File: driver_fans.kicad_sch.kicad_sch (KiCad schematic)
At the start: 0 parts

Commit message: Added drived fan circuitry
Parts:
- added FAN1, FAN2: FANCONN, Connector_Molex:Molex_Micro-Fit_3.0_43650-0215_1x02_P3.00mm_Vertical, symbol Connector_Generic:Conn_01x02
- added Q3 (x2): 2N7002, Package_TO_SOT_SMD:SOT-23, symbol Transistor_FET:2N7002
- added R16: 100k, Resistor_SMD:R_0805_2012Metric, symbol Device:R_Small
- added U2: SI8261ABC-IS, Package_SO:SOIC-8_3.9x4.9mm_P1.27mm, symbol utsvt-bps:SI8261ABC-IS
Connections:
- new net +12V: FAN1.1 (Pin_1), FAN2.1 (Pin_1), U2.8 (VDD)
- new net FAN_SIG_12V_1: FAN1.2 (Pin_2), Q3.3 (D)
- new net FAN_SIG_12V_2: FAN2.2 (Pin_2), Q3.3 (D)
- new net FAN_SIG_3V3: U2.2 (ANODE)
- new net GND: U2.3 (CATHODE)
- new net GNDPWR: Q3.2 (S), Q3.2 (S), R16.1, U2.5 (GND)
- new net VO: Q3.1 (G), Q3.1 (G), R16.2, U2.6 (VO), U2.7 (VO)
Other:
- note added: "Driver Fans"

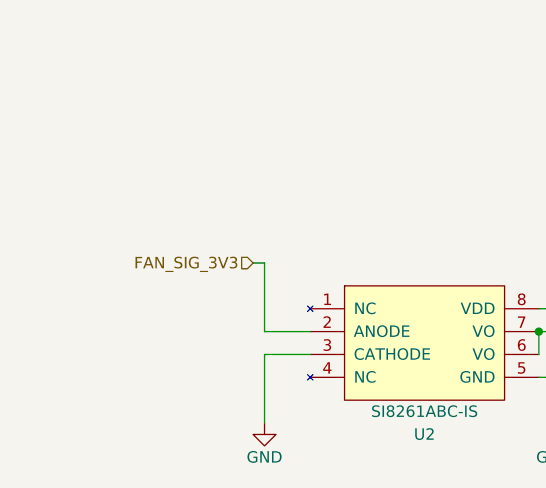
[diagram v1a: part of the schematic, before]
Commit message: Added resistor to fan isolator, fixed ERC errors and warnings
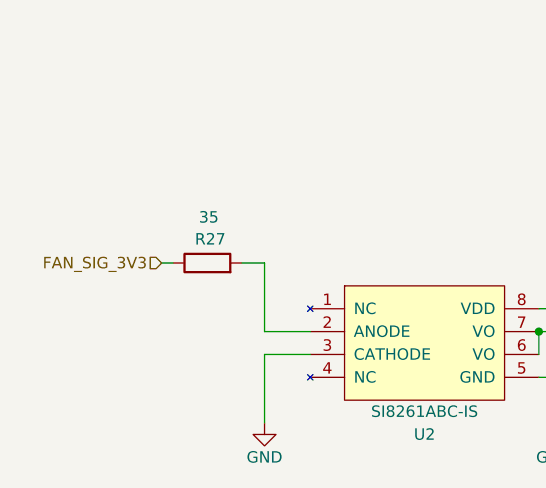
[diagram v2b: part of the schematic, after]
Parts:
- added R27: 35, Resistor_SMD:R_0805_2012Metric, symbol Device:R
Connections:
- net FAN_SIG_3V3: now also R27.1; no longer U2.2 (ANODE)
- new net: R27.2, U2.2 (ANODE)
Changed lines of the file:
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@@
+    (stroke (width 0) (type default))
+  )
+  (wire (pts (xy 57.15 90.17) (xy 58.42 90.17))
     (stroke (width 0) (type default))
   )
@@
     (stroke (width 0) (type default))
   )
-  (wire (pts (xy 67.31 90.17) (xy 68.58 90.17))
+  (wire (pts (xy 66.04 90.17) (xy 68.58 90.17))
     (stroke (width 0) (type default))
   )
@@
     (effects (font (size 1.27 1.27)) (justify right bottom))
   )
-  (hierarchical_label "FAN_SIG_3V3" (shape input) (at 67.31 90.17 180) (fields_autoplaced)
+  (hierarchical_label "FAN_SIG_3V3" (shape input) (at 57.15 90.17 180) (fields_autoplaced)
     (effects (font (size 1.27 1.27)) (justify right))
   )
@@
         )
       )
+    )
+  )
+  (symbol (lib_id "Device:R") (at 62.23 90.17 90) (unit 1)
+    (in_bom yes) (on_board yes) (dnp no)
+    (property "Reference" "R27" (at 64.262 87.5284 90)
+      (effects (font (size 1.27 1.27)) (justify left))
+    )
+    (property "Value" "35" (at 63.5 85.09 90)
+      (effects (font (size 1.27 1.27)) (justify left))
+    )
+    (property "Footprint" "Resistor_SMD:R_0805_2012Metric" (at 62.23 91.948 90)
+      (effects (font (size 1.27 1.27)) hide)
+    )
+    (property "Datasheet" "~" (at 62.23 90.17 0)
+      (effects (font (size 1.27 1.27)) hide)
+    )
+    (property "P/N" "SDR10EZPJ152" (at 62.23 90.17 90)
+      (effects (font (size 1.27 1.27)) hide)
+    )
+    (pin "1")
+    (pin "2")
+    (instances
+      (project "Controls-LightingPCB"
+        (path "/229b82f0-5048-47d6-8bc8-0bcee42eb4bc"
+          (reference "R27") (unit 1)
+        )
+        (path "/229b82f0-5048-47d6-8bc8-0bcee42eb4bc/878def96-76f6-45ed-b005-573a6523d263"
+          (reference "R30") (unit 1)
+        )
+        (path "/229b82f0-5048-47d6-8bc8-0bcee42eb4bc/ceb5a95e-a274-4dea-8a59-96d1af6e854d"
+          (reference "R18") (unit 1)
+        )
+      )
+      (project "Controls-DaughterPCB"
+        (path "/c7871779-04fe-4705-8150-20a4dd0ef44f/f7827f80-0f50-4e4f-b2cd-ff48878538ae"
+          (reference "R16") (unit 1)
+        )
+        (path "/c7871779-04fe-4705-8150-20a4dd0ef44f/fd5723b9-3644-4daa-af29-4c44667f673c"
+          (reference "R32") (unit 1)
+        )
+      )

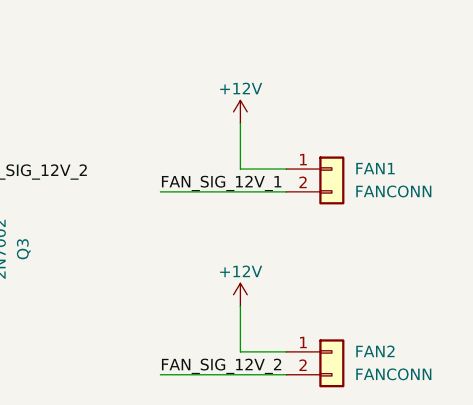
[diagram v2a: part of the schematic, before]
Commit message: changed labels for some connectors
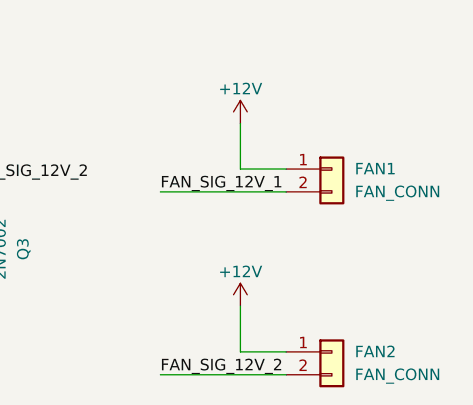
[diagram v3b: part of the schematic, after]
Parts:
- FAN1, FAN2: value FANCONN -> FAN_CONN
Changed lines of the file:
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@@
       (effects (font (size 1.27 1.27)) (justify left))
     )
-    (property "Value" "FANCONN" (at 187.96 91.44 0)
+    (property "Value" "FAN_CONN" (at 187.96 91.44 0)
       (effects (font (size 1.27 1.27)) (justify left))
     )
@@
       (effects (font (size 1.27 1.27)) (justify left))
     )
-    (property "Value" "FANCONN" (at 187.96 111.76 0)
-      (effects (font (size 1.27 1.27)) (justify left))
-    )
+    (property "Value" "FAN_CONN" (at 187.96 111.76 0)
+      (effects (font (size 1.27 1.27)) (justify left))
+    )

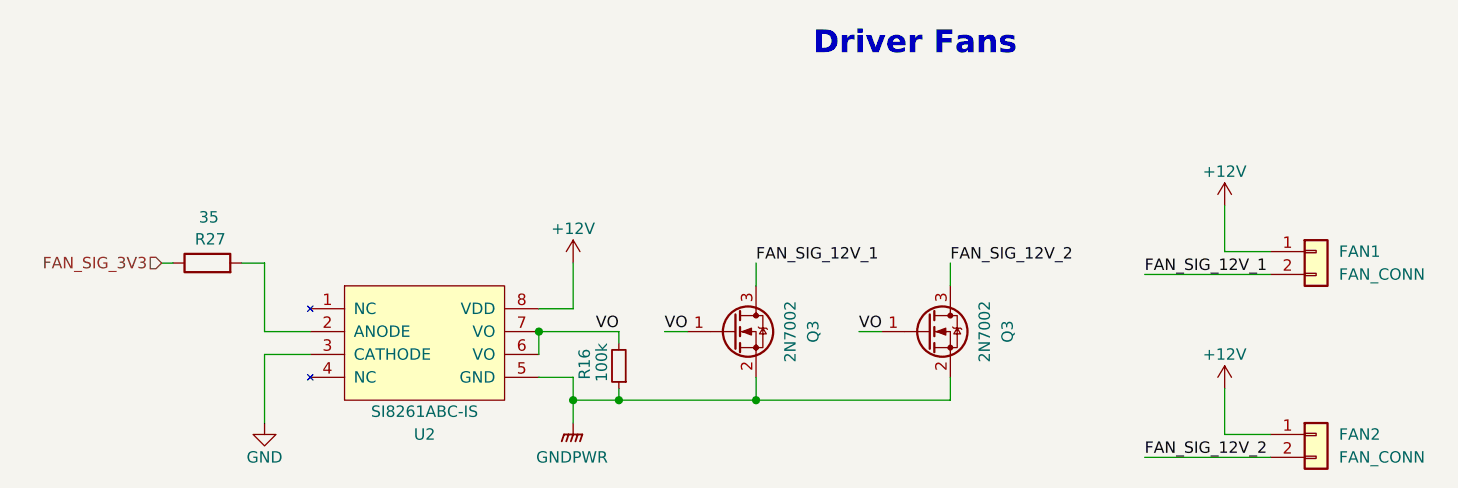
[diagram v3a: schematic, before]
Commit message: lower power optocouplers now used for lights and fans, updated version history
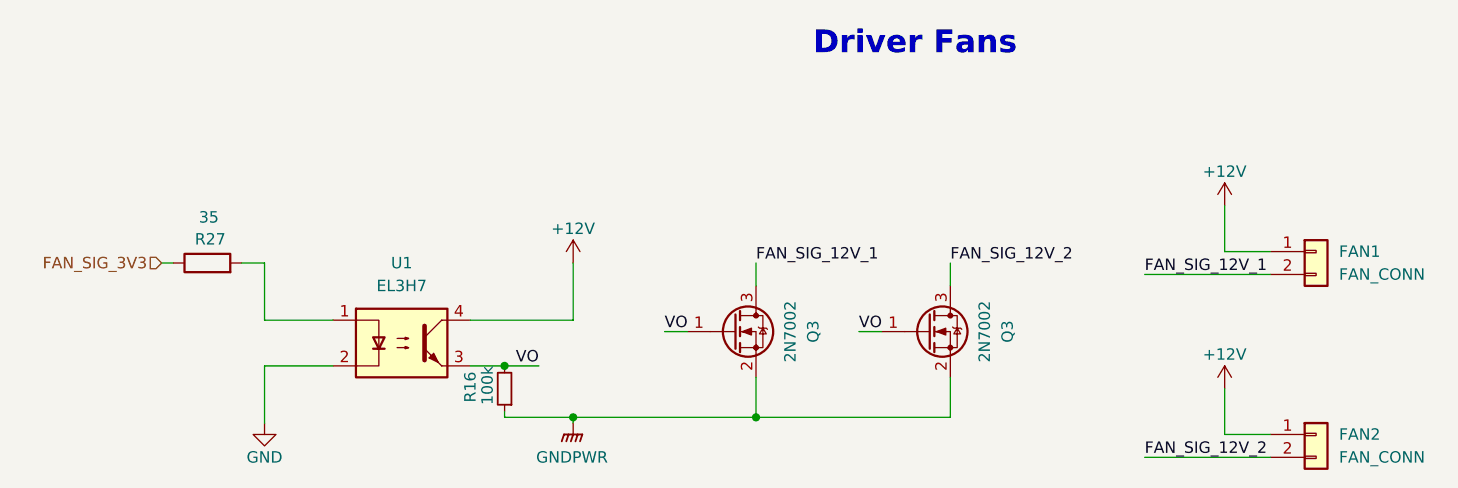
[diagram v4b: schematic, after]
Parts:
- removed U2: SI8261ABC-IS, Package_SO:SOIC-8_3.9x4.9mm_P1.27mm, symbol utsvt-bps:SI8261ABC-IS
- added U1: EL3H7, Package_SO:SOP-4_4.4x2.6mm_P1.27mm, symbol Isolator:EL817
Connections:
- net +12V: now also U1.4
- net GND: now also U1.2
- net VO: now also U1.3
- net at R27.2: now also U1.1
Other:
- moved on the sheet: R16

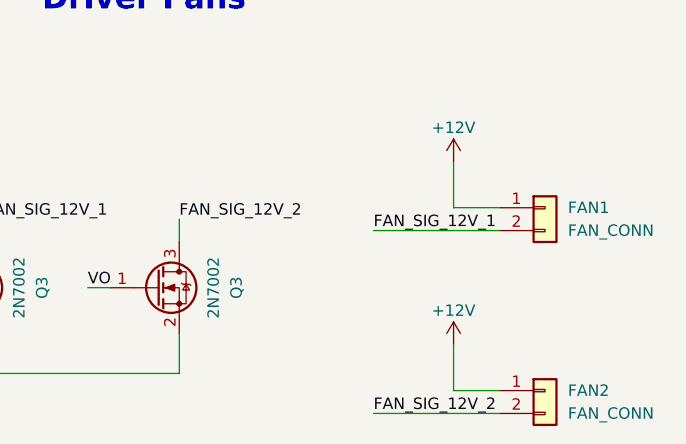
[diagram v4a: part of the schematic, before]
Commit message: Added flyback diodes to fan connectors
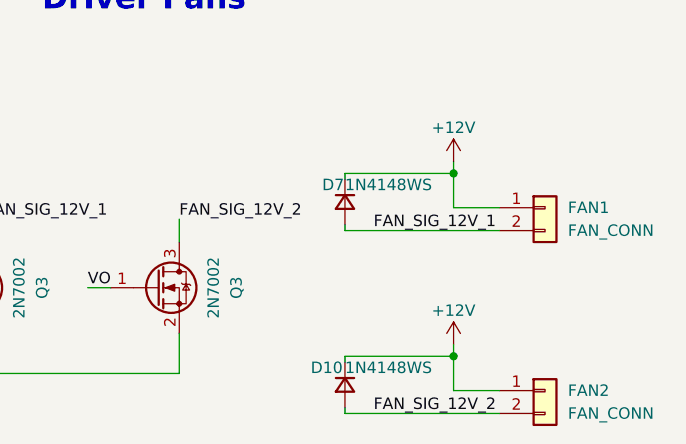
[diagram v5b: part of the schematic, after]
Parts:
- added D10, D7: 1N4148WS, Diode_SMD:D_SOD-323F, symbol Device:D_Small
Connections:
- net +12V: now also D10.1 (K), D7.1 (K)
- net FAN_SIG_12V_1: now also D7.2 (A)
- net FAN_SIG_12V_2: now also D10.2 (A)
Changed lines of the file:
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@@
 (kicad_sch (version 20230121) (generator eeschema)
   (paper "A4")
+  (junction (at 175.26 85.09) (diameter 0) (color 0 0 0 0)
+  )
   (junction (at 95.25 101.6) (diameter 0) (color 0 0 0 0)
   )
@@
   (junction (at 102.87 107.315) (diameter 0) (color 0 0 0 0)
   )
-  (wire (pts (xy 180.34 111.76) (xy 166.37 111.76))
+  (junction (at 175.26 105.41) (diameter 0) (color 0 0 0 0)
+  )
+  (wire (pts (xy 163.195 111.76) (xy 180.34 111.76))
+    (stroke (width 0) (type default))
+  )
+  (wire (pts (xy 163.195 85.09) (xy 163.195 85.725))
+    (stroke (width 0) (type default))
+  )
+  (wire (pts (xy 163.195 105.41) (xy 175.26 105.41))
     (stroke (width 0) (type default))
   )
@@
     (stroke (width 0) (type default))
   )
-  (wire (pts (xy 175.26 104.14) (xy 175.26 109.22))
+  (wire (pts (xy 175.26 104.14) (xy 175.26 105.41))
     (stroke (width 0) (type default))
   )
@@
     (stroke (width 0) (type default))
   )
-  (wire (pts (xy 175.26 83.82) (xy 175.26 88.9))
+  (wire (pts (xy 175.26 83.82) (xy 175.26 85.09))
     (stroke (width 0) (type default))
   )
@@
     (stroke (width 0) (type default))
   )
+  (wire (pts (xy 163.195 105.41) (xy 163.195 106.045))
+    (stroke (width 0) (type default))
+  )
   (wire (pts (xy 144.78 107.315) (xy 144.78 102.87))
     (stroke (width 0) (type default))
@@
     (stroke (width 0) (type default))
   )
+  (wire (pts (xy 163.195 85.09) (xy 175.26 85.09))
+    (stroke (width 0) (type default))
+  )
+  (wire (pts (xy 163.195 111.125) (xy 163.195 111.76))
+    (stroke (width 0) (type default))
+  )
   (wire (pts (xy 91.44 101.6) (xy 95.25 101.6))
     (stroke (width 0) (type default))
@@
     (stroke (width 0) (type default))
   )
+  (wire (pts (xy 175.26 105.41) (xy 175.26 109.22))
+    (stroke (width 0) (type default))
+  )
+  (wire (pts (xy 163.195 90.805) (xy 163.195 91.44))
+    (stroke (width 0) (type default))
+  )
+  (wire (pts (xy 175.26 85.09) (xy 175.26 88.9))
+    (stroke (width 0) (type default))
+  )
   (wire (pts (xy 102.87 107.315) (xy 102.87 107.95))
     (stroke (width 0) (type default))
   )
-  (wire (pts (xy 180.34 91.44) (xy 166.37 91.44))
+  (wire (pts (xy 163.195 91.44) (xy 180.34 91.44))
     (stroke (width 0) (type default))
   )
@@
     )
   )
+  (symbol (lib_id "Device:D_Small") (at 163.195 108.585 270) (unit 1)
+    (in_bom yes) (on_board yes) (dnp no)
+    (property "Reference" "D10" (at 159.385 106.68 90)
+      (effects (font (size 1.27 1.27)) (justify left))
+    )
+    (property "Value" "1N4148WS" (at 163.195 106.68 90)
+      (effects (font (size 1.27 1.27)) (justify left))
+    )
+    (property "Footprint" "Diode_SMD:D_SOD-323F" (at 163.195 108.585 90)
+      (effects (font (size 1.27 1.27)) hide)
+    )
+    (property "Datasheet" "https://www.mouser.com/datasheet/2/849/1n4148ws-3323949.pdf" (at 163.195 108.585 90)
+      (effects (font (size 1.27 1.27)) hide)
+    )
+    (property "Sim.Device" "D" (at 163.195 108.585 0)
+      (effects (font (size 1.27 1.27)) hide)
+    )
+    (property "Sim.Pins" "1=K 2=A" (at 163.195 108.585 0)
+      (effects (font (size 1.27 1.27)) hide)
+    )
+    (property "PN" "1N4148WS" (at 163.195 108.585 90)
+      (effects (font (size 1.27 1.27)) hide)
+    )
+    (property "Mouser #" "637-1N4148WS" (at 163.195 108.585 90)
+      (effects (font (size 1.27 1.27)) hide)
+    )
+    (pin "1")
+    (pin "2")
+    (instances
+      (project "Controls-LeaderDaughterPCB"
+        (path "/c7871779-04fe-4705-8150-20a4dd0ef44f/fd5723b9-3644-4daa-af29-4c44667f673c"
+          (reference "D10") (unit 1)
+        )
+      )
+    )
+  )
   (symbol (lib_id "power:+12V") (at 102.87 90.17 0) (unit 1)
     (in_bom yes) (on_board yes) (dnp no)
@@
         )
       )
+    )
+  )
+  (symbol (lib_id "Device:D_Small") (at 163.195 88.265 270) (unit 1)
+    (in_bom yes) (on_board yes) (dnp no)
+    (property "Reference" "D7" (at 160.655 86.36 90)
+      (effects (font (size 1.27 1.27)) (justify left))
+    )
+    (property "Value" "1N4148WS" (at 163.195 86.36 90)
+      (effects (font (size 1.27 1.27)) (justify left))
+    )
+    (property "Footprint" "Diode_SMD:D_SOD-323F" (at 163.195 88.265 90)
+      (effects (font (size 1.27 1.27)) hide)
+    )
+    (property "Datasheet" "https://www.mouser.com/datasheet/2/849/1n4148ws-3323949.pdf" (at 163.195 88.265 90)
+      (effects (font (size 1.27 1.27)) hide)
+    )
+    (property "Sim.Device" "D" (at 163.195 88.265 0)
+      (effects (font (size 1.27 1.27)) hide)
+    )
+    (property "Sim.Pins" "1=K 2=A" (at 163.195 88.265 0)
+      (effects (font (size 1.27 1.27)) hide)
+    )
+    (property "PN" "1N4148WS" (at 163.195 88.265 90)
+      (effects (font (size 1.27 1.27)) hide)
+    )
+    (property "Mouser #" "637-1N4148WS" (at 163.195 88.265 90)
+      (effects (font (size 1.27 1.27)) hide)
+    )
+    (pin "1")
+    (pin "2")
+    (instances
+      (project "Controls-LeaderDaughterPCB"
+        (path "/c7871779-04fe-4705-8150-20a4dd0ef44f/fd5723b9-3644-4daa-af29-4c44667f673c"
+          (reference "D7") (unit 1)
+        )
+      )

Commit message: updated footprints and part numbers, added motor CAN 12V connection
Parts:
- D10, D7: Mauser PN (none) -> 637-1N4148WS; Mouser # 637-1N4148WS -> (none)
- FAN1, FAN2: Mauser PN (none) -> 538-43650-0415; PN (none) -> 43650-0215
- Q3: Mauser PN (none) -> 771-2N7002HR; P/N 2N7002HR -> (none); PN (none) -> 2N7002HR
- R16: Mauser PN (none) -> 71-CRCW0805100KFKEAC; P/N CRCW0805100KFKEAC -> (none); PN (none) -> CRCW0805100KFKEAC
- R27: Mauser PN (none) -> 791-WR08X35R2FTL; P/N SDR10EZPJ152 -> (none); PN (none) -> WR08X35R2FTL
- U1: Mauser PN (none) -> 638-EL3H7DTAVG; Mouser Part Number 638-EL3H7DTAVG -> (none); PN (none) -> EL3H7(D)(TA)-VG
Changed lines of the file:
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@@
+      (effects (font (size 1.27 1.27)) hide)
+    )
+    (property "PN" "43650-0215" (at 185.42 88.9 0)
+      (effects (font (size 1.27 1.27)) hide)
+    )
+    (property "Mauser PN" "538-43650-0415" (at 185.42 88.9 0)
       (effects (font (size 1.27 1.27)) hide)
     )
@@
       (effects (font (size 1.27 1.27)) hide)
     )
-    (property "Datasheet" "~" (at 95.25 104.14 0)
-      (effects (font (size 1.27 1.27)) hide)
-    )
-    (property "P/N" "CRCW0805100KFKEAC" (at 95.25 104.14 0)
+    (property "Datasheet" "https://www.vishay.com/docs/28773/crcwce3.pdf" (at 95.25 104.14 0)
+      (effects (font (size 1.27 1.27)) hide)
+    )
+    (property "PN" "CRCW0805100KFKEAC" (at 95.25 104.14 0)
+      (effects (font (size 1.27 1.27)) hide)
+    )
+    (property "Mauser PN" "71-CRCW0805100KFKEAC" (at 95.25 104.14 0)
       (effects (font (size 1.27 1.27)) hide)
     )
@@
       (effects (font (size 1.27 1.27)) hide)
     )
-    (property "Datasheet" "~" (at 62.23 90.17 0)
-      (effects (font (size 1.27 1.27)) hide)
-    )
-    (property "P/N" "SDR10EZPJ152" (at 62.23 90.17 90)
+    (property "Datasheet" "https://www.mouser.com/datasheet/2/210/ASC_WR-3314721.pdf" (at 62.23 90.17 0)
+      (effects (font (size 1.27 1.27)) hide)
+    )
+    (property "PN" "WR08X35R2FTL" (at 62.23 90.17 0)
+      (effects (font (size 1.27 1.27)) hide)
+    )
+    (property "Mauser PN" "791-WR08X35R2FTL" (at 62.23 90.17 0)
       (effects (font (size 1.27 1.27)) hide)
     )
@@
       (effects (font (size 1.27 1.27) italic) (justify left) hide)
     )
-    (property "Datasheet" "https://www.onsemi.com/pub/Collateral/NDS7002A-D.PDF" (at 120.65 97.79 0)
+    (property "Datasheet" "https://www.mouser.com/datasheet/2/916/2N7002H-2909812.pdf" (at 120.65 97.79 0)
       (effects (font (size 1.27 1.27)) (justify left) hide)
     )
-    (property "P/N" "2N7002HR" (at 120.65 97.79 90)
+    (property "PN" "2N7002HR" (at 120.65 97.79 0)
+      (effects (font (size 1.27 1.27)) hide)
+    )
+    (property "Mauser PN" "771-2N7002HR" (at 120.65 97.79 0)
       (effects (font (size 1.27 1.27)) hide)
     )
@@
       (effects (font (size 1.27 1.27)) (justify left) hide)
     )
-    (property "Mouser Part Number" "638-EL3H7DTAVG " (at 83.82 99.06 90)
+    (property "Mauser PN" "638-EL3H7DTAVG " (at 83.82 99.06 0)
+      (effects (font (size 1.27 1.27)) hide)
+    )
+    (property "PN" "EL3H7(D)(TA)-VG" (at 83.82 99.06 0)
       (effects (font (size 1.27 1.27)) hide)
     )
@@
       (effects (font (size 1.27 1.27) italic) (justify left) hide)
     )
-    (property "Datasheet" "https://www.onsemi.com/pub/Collateral/NDS7002A-D.PDF" (at 142.24 97.79 0)
+    (property "Datasheet" "https://www.mouser.com/datasheet/2/916/2N7002H-2909812.pdf" (at 142.24 97.79 0)
       (effects (font (size 1.27 1.27)) (justify left) hide)
     )
-    (property "P/N" "2N7002HR" (at 142.24 97.79 90)
+    (property "PN" "2N7002HR" (at 142.24 97.79 0)
+      (effects (font (size 1.27 1.27)) hide)
+    )
+    (property "Mauser PN" "771-2N7002HR" (at 142.24 97.79 0)
       (effects (font (size 1.27 1.27)) hide)
     )
@@
       (effects (font (size 1.27 1.27)) hide)
     )
-    (property "Mouser #" "637-1N4148WS" (at 163.195 108.585 90)
+    (property "Mauser PN" "637-1N4148WS" (at 163.195 108.585 0)
       (effects (font (size 1.27 1.27)) hide)
     )
@@
       (effects (font (size 1.27 1.27)) hide)
     )
-    (property "Mouser #" "637-1N4148WS" (at 163.195 88.265 90)
+    (property "Mauser PN" "637-1N4148WS" (at 163.195 88.265 0)
       (effects (font (size 1.27 1.27)) hide)
     )
@@
       (effects (font (size 1.27 1.27)) hide)
     )
+    (property "PN" "43650-0215" (at 185.42 109.22 0)
+      (effects (font (size 1.27 1.27)) hide)
+    )
+    (property "Mauser PN" "538-43650-0415" (at 185.42 109.22 0)
+      (effects (font (size 1.27 1.27)) hide)
+    )
